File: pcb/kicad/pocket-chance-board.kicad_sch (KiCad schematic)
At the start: 132 parts, among them J1 SWD, J2 USB4085-GF-A, J3 LiPo JST-PH 2.0mm (1 = + RED,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, J4 LCD 1.54in ST7789 module, JST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, J5 Speaker JST-PH, J6 microSD Molex 104031-0811, J7 STEMMA QT, J8 Expansion (6 = VBAT_SENSE ADC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, Q1 FS8205A, Q3 AO3400A, Q4 AO3401A, SW1 BOOT, SW10 DPAD LEFT PTS645SM43SMTR92, SW11 DPAD RIGHT PTS645SM43SMTR92, SW12 DPAD PRESS PTS645SM43SMTR92, SW2 RESET, SW3 POWER PCM12, SW4 A PTS125SM43SMTR2LFS, SW5 B PTS125SM43SMTR2LFS, SW6 X PTS125SM43SMTR2LFS, SW7 Y PTS125SM43SMTR2LFS, SW8 DPAD UP PTS645SM43SMTR92, SW9 DPAD DOWN PTS645SM43SMTR92, U1 RP2350A, U10 LSM6DSOXTR, U11 RM2, U2 W25Q128JVSIQ, U3 APS6404L-3SQR-SN, U4 USBLC6-2SC6, U5 BQ24074RGTR, U6 TPS63001DRCR, U7 DW01A, U8 PAM8302AADCR, U9 DS3231MZ+, Y1 12MHz ABM8-272-T3

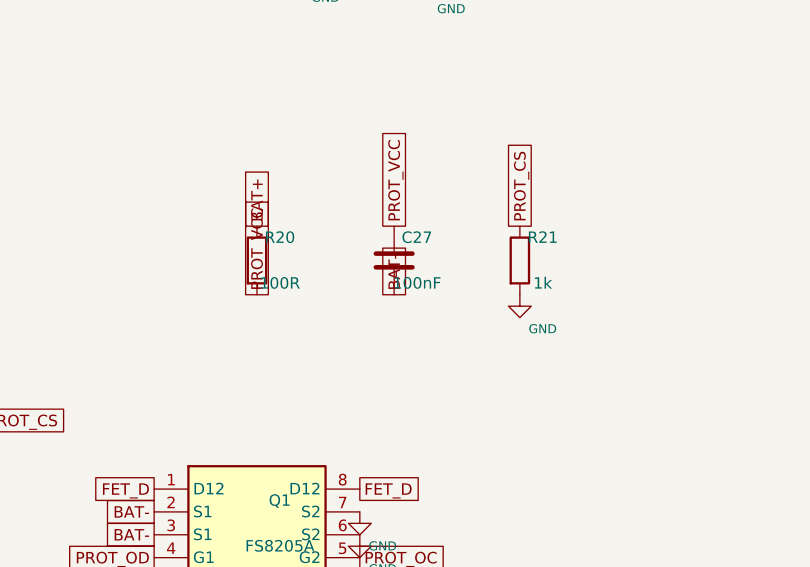
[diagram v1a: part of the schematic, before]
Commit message: Rev 0.8: DW01A resistors per its datasheet (R20 470 ohm, was 100 below the required minimum; R21 2 k); DW01A pin map and thresholds recorded
Co-Authored-By: Claude Fable 5.1 <noreply@anthropic.com>
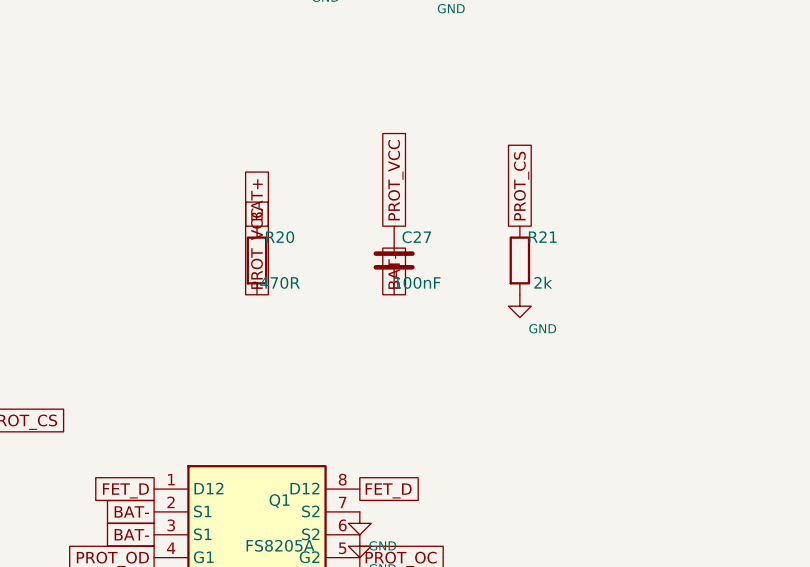
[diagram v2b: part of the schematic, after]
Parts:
- R20: value 100R -> 470R; footprint Resistor_SMD:R_0603_1608Metric -> Resistor_SMD:R_0402_1005Metric
- R21: value 1k -> 2k
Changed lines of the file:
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@@
 		(title "Pocket Chance board, spin 1")
 		(date "2026-10-04")
-		(rev "0.7")
+		(rev "0.8")
 		(company "Pocket Chance")
 		(comment 1 "Generated by pcb/tools/gen_sch.py from the connection table. Label-based: every pin carries its net name.")
@@
 			)
 		)
-		(property "Value" "100R"
+		(property "Value" "470R"
 			(at 342.9 337.82 0)
 			(effects
@@
 			)
 		)
-		(property "Footprint" "Resistor_SMD:R_0603_1608Metric"
+		(property "Footprint" "Resistor_SMD:R_0402_1005Metric"
 			(at 340.36 335.28 0)
 			(effects
@@
 			)
 		)
-		(property "Value" "1k"
+		(property "Value" "2k"
 			(at 372.11 337.82 0)
 			(effects

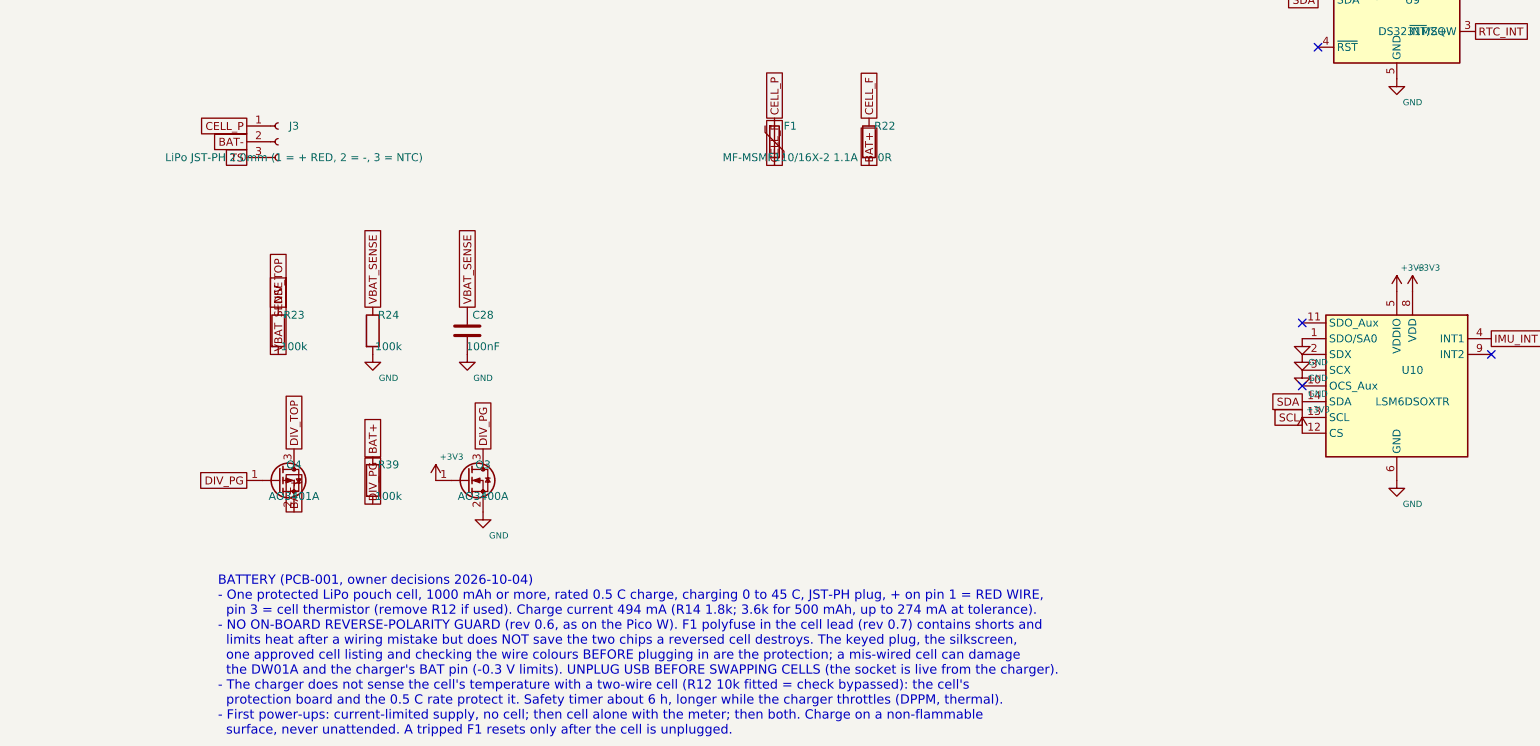
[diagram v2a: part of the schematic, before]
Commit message: Rev 0.9: 2-pin battery socket (thermistor pin dropped) and 1.5 A polyfuse, John's rulings
Co-Authored-By: Claude Fable 5.1 <noreply@anthropic.com>
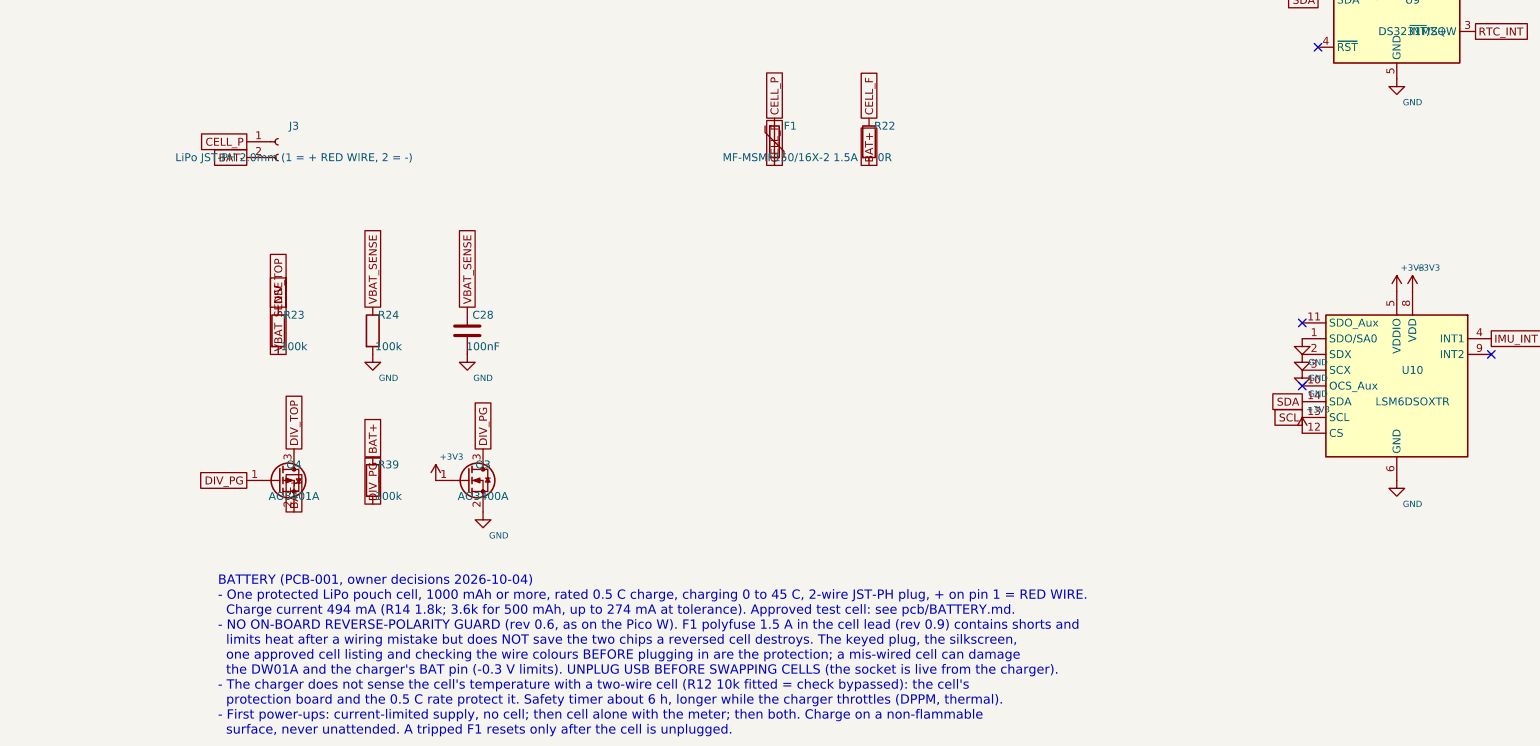
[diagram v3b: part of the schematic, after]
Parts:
- removed J3: LiPo JST-PH 2.0mm (1 = + RED, 2 = -, 3 = NTC), Connector_JST:JST_PH_S3B-PH-SM4-TB_1x03-1MP_P2.00mm_Horizontal, symbol Connector:Conn_01x03_Socket
- added J3: LiPo JST-PH 2.0mm (1 = + RED WIRE, 2 = -), Connector_JST:JST_PH_S2B-PH-SM4-TB_1x02-1MP_P2.00mm_Horizontal, symbol Connector:Conn_01x02_Socket
- F1: value MF-MSMF110/16X-2 1.1A -> MF-MSMF150/16X-2 1.5A
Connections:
- net BAT-: now also J3.2 (Pin_2)
- net CELL_P: now also J3.1 (Pin_1)
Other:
- note added: "BATTERY (PCB-001, owner decisions 2026-10-04) - One protected LiPo pouch cell, 1000 mAh or more, rated 0.5 C charge, charging 0 to 45 C, 2-wire JST-PH plug, + on pin 1 = RED WIRE. Charge current 494 mA (R14 1.8k; 3.6k for 500 mAh, up to 274 mA at tolerance). Approved test cell: see pcb/BATTERY.md. - NO ON-BOARD REVERSE-POLARITY GUARD (rev 0.6, as on the Pico W). F1 polyfuse 1.5 A in the cell lead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"
- note removed: "BATTERY (PCB-001, owner decisions 2026-10-04) - One protected LiPo pouch cell, 1000 mAh or more, rated 0.5 C charge, charging 0 to 45 C, JST-PH plug, + on pin 1 = RED WIRE, pin 3 = cell thermistor (remove R12 if used). Charge current 494 mA (R14 1.8k; 3.6k for 500 mAh, up to 274 mA at tolerance). - NO ON-BOARD REVERSE-POLARITY GUARD (rev 0.6, as on the Pico W). F1 polyfuse in the cell lead (rev 0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"
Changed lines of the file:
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@@
 		(title "Pocket Chance board, spin 1")
 		(date "2026-10-04")
-		(rev "0.8")
+		(rev "0.9")
 		(company "Pocket Chance")
 		(comment 1 "Generated by pcb/tools/gen_sch.py from the connection table. Label-based: every pin carries its net name.")
@@
 	)
 	(symbol
-		(lib_id "Connector:Conn_01x03_Socket")
+		(lib_id "Connector:Conn_01x02_Socket")
 		(at 299.72 400.05 0)
 		(unit 1)
@@
 			)
 		)
-		(property "Value" "LiPo JST-PH 2.0mm (1 = + RED, 2 = -, 3 = NTC)"
+		(property "Value" "LiPo JST-PH 2.0mm (1 = + RED WIRE, 2 = -)"
 			(at 302.26 402.59 0)
 			(effects
@@
 			)
 		)
-		(property "Footprint" "Connector_JST:JST_PH_S3B-PH-SM4-TB_1x03-1MP_P2.00mm_Horizontal"
+		(property "Footprint" "Connector_JST:JST_PH_S2B-PH-SM4-TB_1x02-1MP_P2.00mm_Horizontal"
 			(at 299.72 400.05 0)
 			(effects
@@
 		(pin "2"
 		)
-		(pin "3"
-		)
 		(instances
 			(project "pocket-chance-board"
@@
 	(global_label "CELL_P"
 		(shape passive)
-		(at 294.64 397.51 180)
-		(fields_autoplaced yes)
-		(effects
-			(font
-				(size 1.27 1.27)
-			)
-			(justify right)
-		)
-		(property "Intersheetrefs" "${INTERSHEET_REFS}"
-			(at 294.64 397.51 0)
-			(effects
-				(font
-					(size 1.27 1.27)
-				)
-				hide
-			)
-		)
-	)
-	(global_label "BAT-"
-		(shape passive)
 		(at 294.64 400.05 180)
 		(fields_autoplaced yes)
@@
 		)
 	)
-	(global_label "TS"
+	(global_label "BAT-"
 		(shape passive)
 		(at 294.64 402.59 180)
@@
 			)
 		)
-		(property "Value" "MF-MSMF110/16X-2 1.1A"
+		(property "Value" "MF-MSMF150/16X-2 1.5A"
 			(at 382.27 402.59 0)
 			(effects
@@
 		)
 	)
-	(text "BATTERY (PCB-001, owner decisions 2026-10-04)\n- One protected LiPo pouch cell, 1000 mAh or more, rated 0.5 C charge, charging 0 to 45 C, JST-PH plug, + on pin 1 = RED WIRE,\n  pin 3 = cell thermistor (remove R12 if used). Charge current 494 mA (R14 1.8k; 3.6k for 500 mAh, up to 274 mA at tolerance).\n- NO ON-BOARD REVERSE-POLARITY GUARD (rev 0.6, as on the Pico W). F1 polyfuse in the cell lead (rev 0.7) contains shorts and\n  limits heat after a wiring mistake but does NOT save the two chips a reversed cell destroys. The keyed plug, the silkscreen,\n  one approved cell listing and checking the wire colours BEFORE plugging in are the protection; a mis-wired cell can damage\n  the DW01A and the charger's BAT pin (-0.3 V limits). UNPLUG USB BEFORE SWAPPING CELLS (the socket is live from the charger).\n- The charger does not sense the cell's temperature with a two-wire cell (R12 10k fitted = check bypassed): the cell's\n  protection board and the 0.5 C rate protect it. Safety timer about 6 h, longer while the charger throttles (DPPM, thermal).\n- First power-ups: current-limited supply, no cell; then cell alone with the meter; then both. Charge on a non-flammable\n  surface, never unattended. A tripped F1 resets only after the cell is unplugged."
+	(text "BATTERY (PCB-001, owner decisions 2026-10-04)\n- One protected LiPo pouch cell, 1000 mAh or more, rated 0.5 C charge, charging 0 to 45 C, 2-wire JST-PH plug, + on pin 1 = RED WIRE.\n  Charge current 494 mA (R14 1.8k; 3.6k for 500 mAh, up to 274 mA at tolerance). Approved test cell: see pcb/BATTERY.md.\n- NO ON-BOARD REVERSE-POLARITY GUARD (rev 0.6, as on the Pico W). F1 polyfuse 1.5 A in the cell lead (rev 0.9) contains shorts and\n  limits heat after a wiring mistake but does NOT save the two chips a reversed cell destroys. The keyed plug, the silkscreen,\n  one approved cell listing and checking the wire colours BEFORE plugging in are the protection; a mis-wired cell can damage\n  the DW01A and the charger's BAT pin (-0.3 V limits). UNPLUG USB BEFORE SWAPPING CELLS (the socket is live from the charger).\n- The charger does not sense the cell's temperature with a two-wire cell (R12 10k fitted = check bypassed): the cell's\n  protection board and the 0.5 C rate protect it. Safety timer about 6 h, longer while the charger throttles (DPPM, thermal).\n- First power-ups: current-limited supply, no cell; then cell alone with the meter; then both. Charge on a non-flammable\n  surface, never unattended. A tripped F1 resets only after the cell is unplugged."
 		(exclude_from_sim no)
 		(at 290 470 0)

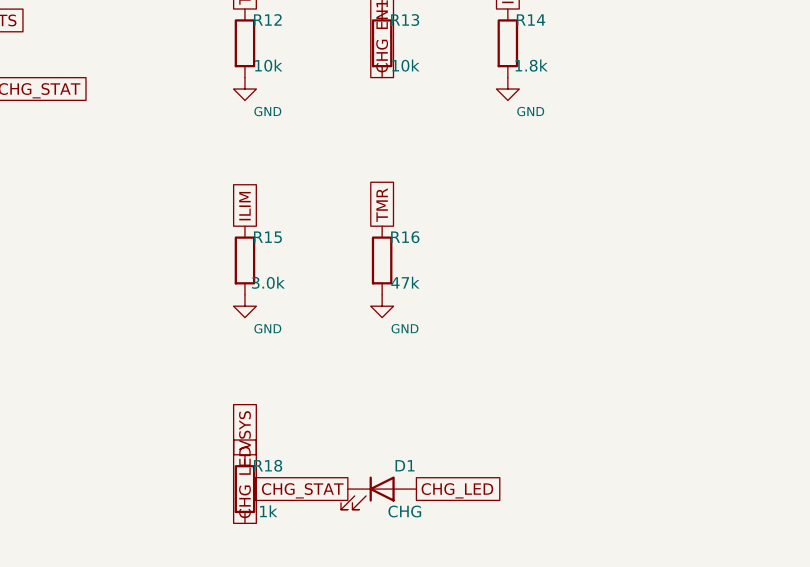
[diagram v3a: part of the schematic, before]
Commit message: Rev 0.10: R16 charge timer 47k to 68k (John's ruling)
Value only. BQ24074 t_MAXCHG 6.8/9.1/11.3 h, so a 2000 mAh charge always completes.

Co-Authored-By: Claude Opus 5.5 <noreply@anthropic.com>
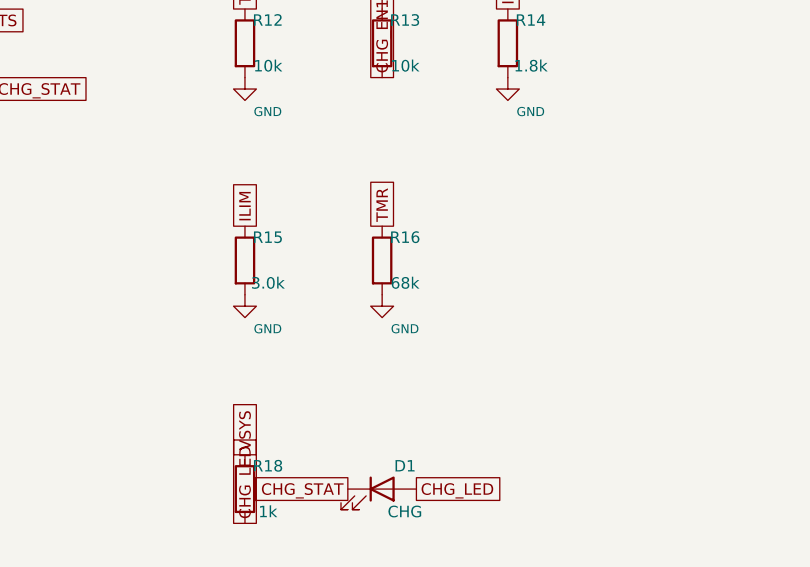
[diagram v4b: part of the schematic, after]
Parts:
- R16: value 47k -> 68k
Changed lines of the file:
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@@
 		(title "Pocket Chance board, spin 1")
 		(date "2026-10-04")
-		(rev "0.9")
+		(rev "0.10")
 		(company "Pocket Chance")
 		(comment 1 "Generated by pcb/tools/gen_sch.py from the connection table. Label-based: every pin carries its net name.")
@@
 			)
 		)
-		(property "Value" "47k"
+		(property "Value" "68k"
 			(at 358.14 212.09 0)
 			(effects

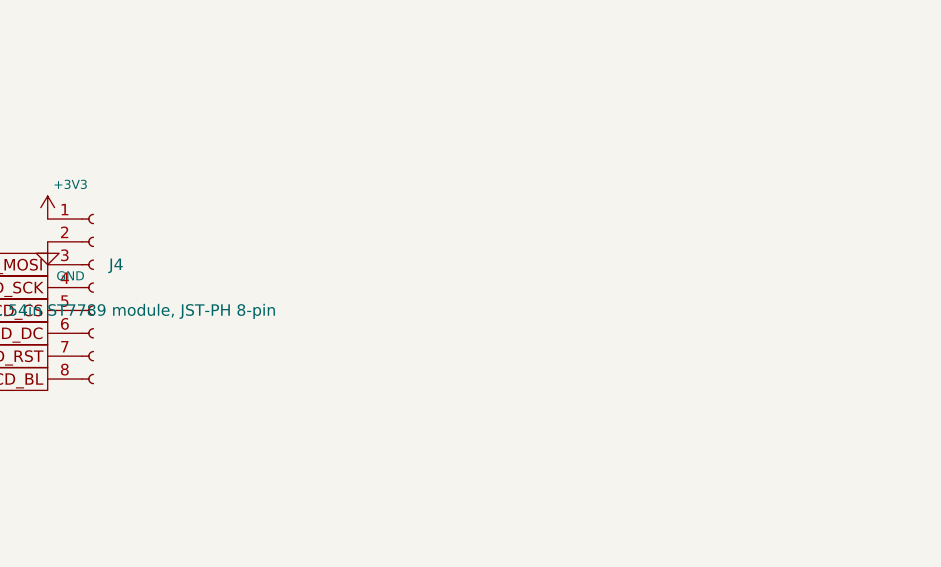
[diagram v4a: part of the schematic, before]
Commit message: Rev 0.11 prep (NOT for merge until John's go): J9 1x8 2.54 mm screen header on J4's nets, pins named on silk
John's ruling (option B) via the PM. Netlist diff vs pcb-design: only J9 added, on +3V3, GND, LCD_MOSI,
LCD_SCK, LCD_CS, LCD_DC, LCD_RST, LCD_BL. ERC 0 errors, 2 expected warnings. Placed between the screen
reserve and J4 at y 44; DRC: no placement errors. The rest of rev 0.11 (probe pads, F1 footprint,
ADC cap) waits for John.

Co-Authored-By: Claude Opus 5.5 <noreply@anthropic.com>
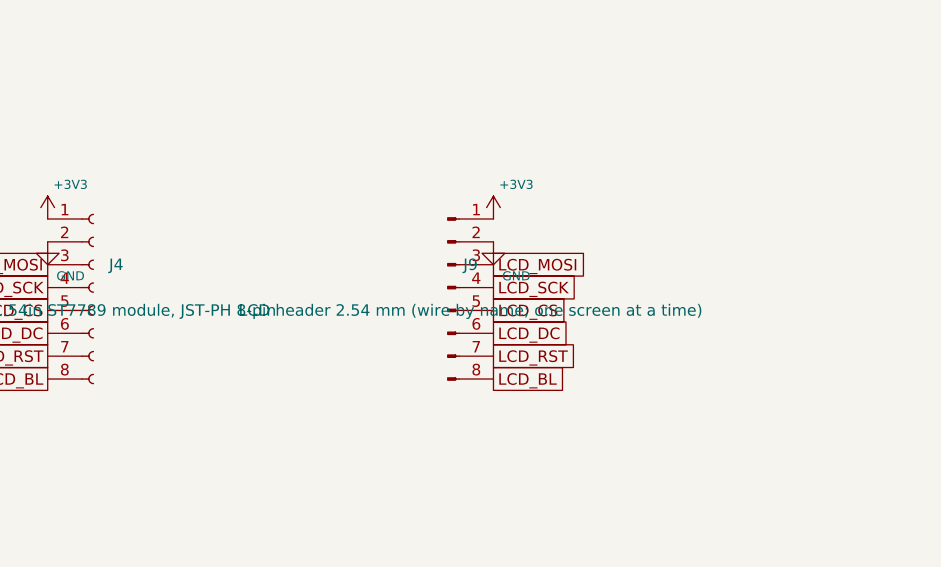
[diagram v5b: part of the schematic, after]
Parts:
- added J9: LCD header 2.54 mm (wire by name; one screen at a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, Connector_PinHeader_2.54mm:PinHeader_1x08_P2.54mm_Vertical, symbol Connector:Conn_01x08_Pin
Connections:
- net +3V3: now also J9.1 (Pin_1)
- net GND: now also J9.2 (Pin_2)
- net LCD_BL: now also J9.8 (Pin_8)
- net LCD_CS: now also J9.5 (Pin_5)
- net LCD_DC: now also J9.6 (Pin_6)
- net LCD_MOSI: now also J9.3 (Pin_3)
- net LCD_RST: now also J9.7 (Pin_7)
- net LCD_SCK: now also J9.4 (Pin_4)

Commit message: Rev 0.11 (John's 'yes all'): J9 screen header, probe pads TP9-TP14, F1 Bourns footprint, C43 ADC 100 nF, backlight link R49 with unfitted Q6/R50/R51
- GPIO13 now net LCD_BL_CTL, joined to LCD_BL by R49 0 ohm (fitted): behaviour unchanged
- Q6 AO3401A high-side switch + R50 1k + R51 100k DNP, for a direct-drive BL module (then BL active LOW)
- netlist diff vs rev 0.10: 12 parts added, F1 footprint field changed, LCD_BL split; nothing removed
- ERC 0 errors, 2 expected warnings; 144 parts placed; placement DRC clean

Co-Authored-By: Claude Opus 5.5 <noreply@anthropic.com>
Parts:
- added C43: 100nF, Capacitor_SMD:C_0402_1005Metric, symbol Device:C
- added Q6: AO3401A (DNP: fit only for a direct-drive BL modu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, Package_TO_SOT_SMD:SOT-23, symbol Transistor_FET:AO3401A
- added R49: 0R, Resistor_SMD:R_0402_1005Metric, symbol Device:R
- added R50: 1k, Resistor_SMD:R_0402_1005Metric, symbol Device:R
- added R51: 100k, Resistor_SMD:R_0402_1005Metric, symbol Device:R
- added TP10: CELL_F, TestPoint:TestPoint_Pad_D1.5mm, symbol Connector:TestPoint
- added TP11: SDA, TestPoint:TestPoint_Pad_D1.5mm, symbol Connector:TestPoint
- added TP12: SCL, TestPoint:TestPoint_Pad_D1.5mm, symbol Connector:TestPoint
- added TP13: SD_SCK, TestPoint:TestPoint_Pad_D1.5mm, symbol Connector:TestPoint
- added TP14: LCD_SCK, TestPoint:TestPoint_Pad_D1.5mm, symbol Connector:TestPoint
- added TP9: CELL_P, TestPoint:TestPoint_Pad_D1.5mm, symbol Connector:TestPoint
- F1: footprint Fuse:Fuse_1812_4532Metric -> pcb_custom:Fuse_Bourns_MF-MSMF_1812
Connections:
- net +3V3: now also Q6.2 (S), R51.1
- net ADC_AVDD: now also C43.1
- net CELL_F: now also TP10.1
- net CELL_P: now also TP9.1
- net GND: now also C43.2
- net LCD_BL: now also Q6.3 (D), R49.2; no longer U1.17 (GPIO13)
- net LCD_SCK: now also TP14.1
- net SCL: now also TP12.1
- net SDA: now also TP11.1
- net SD_SCK: now also TP13.1
- new net BL_GATE: Q6.1 (G), R50.2, R51.2
- new net LCD_BL_CTL: R49.1, R50.1, U1.17 (GPIO13)
